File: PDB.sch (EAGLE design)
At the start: 66 parts

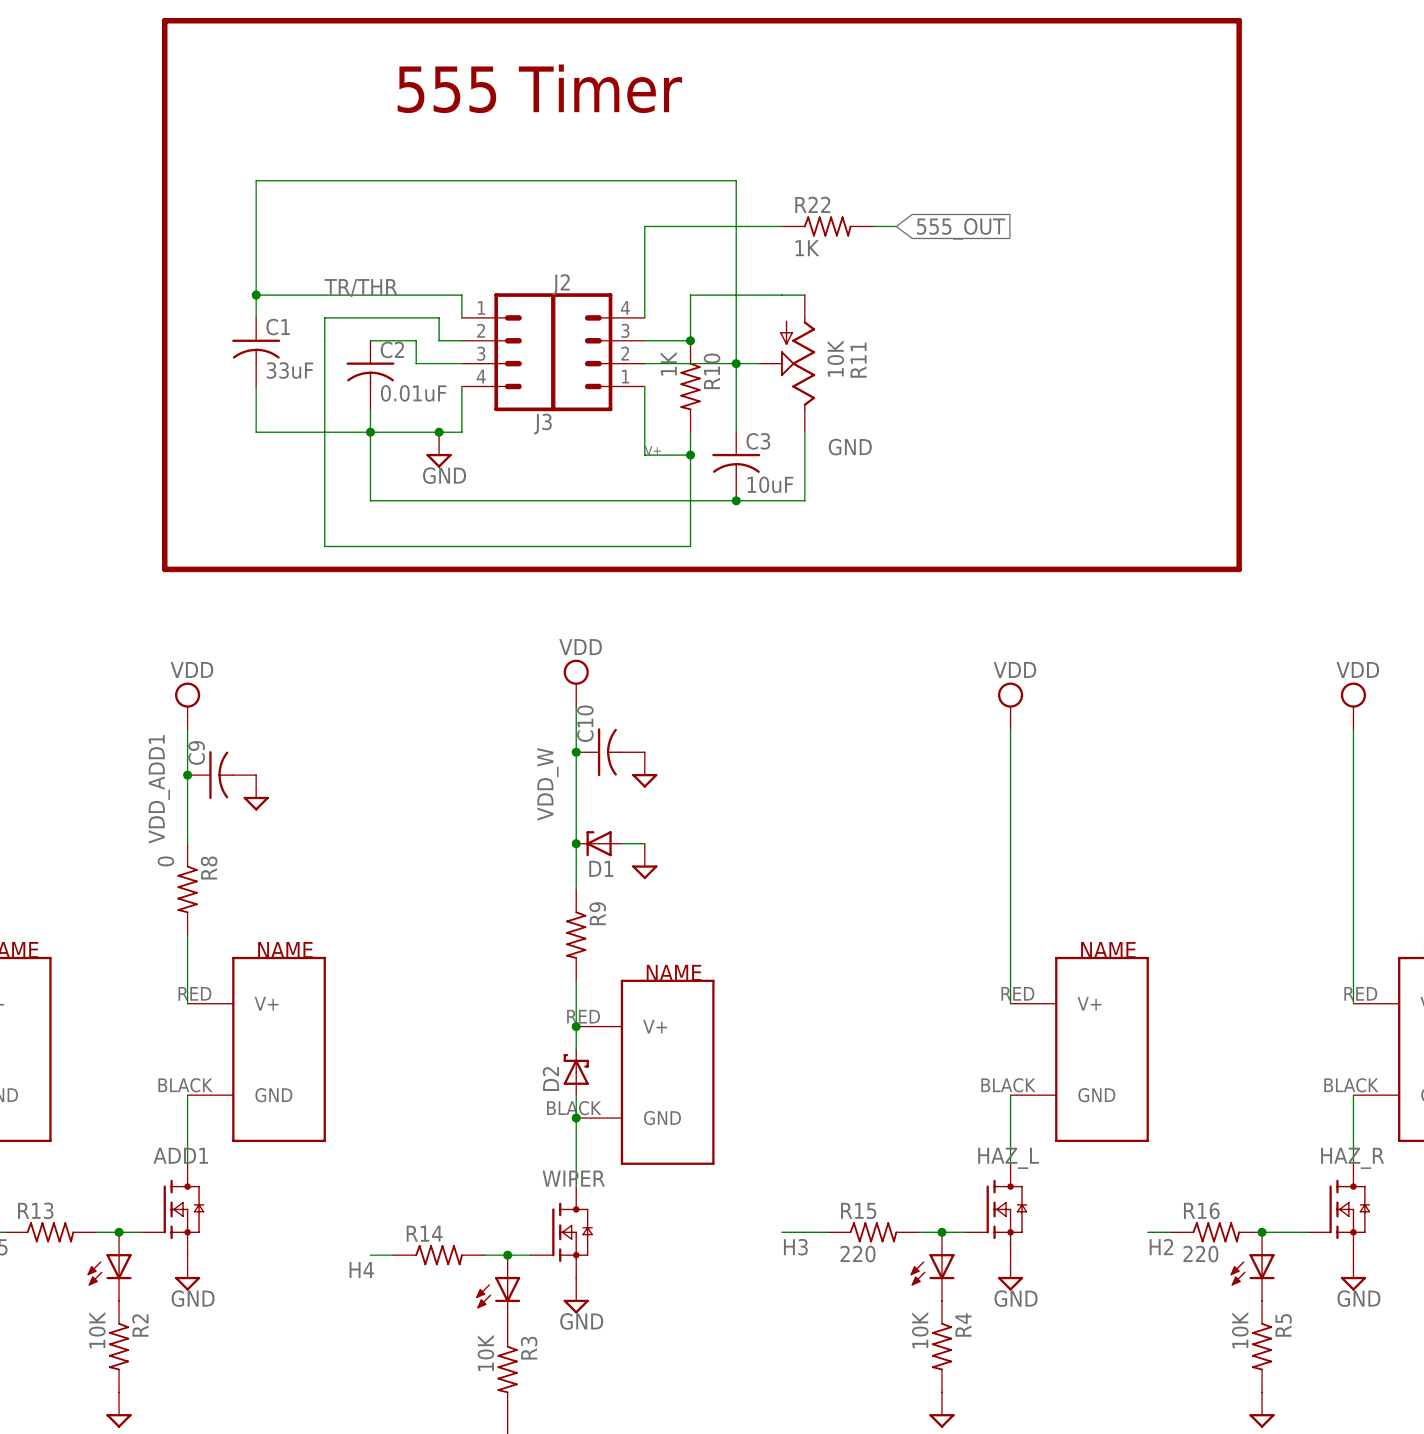
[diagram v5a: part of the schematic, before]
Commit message: modified ground plane in PDB
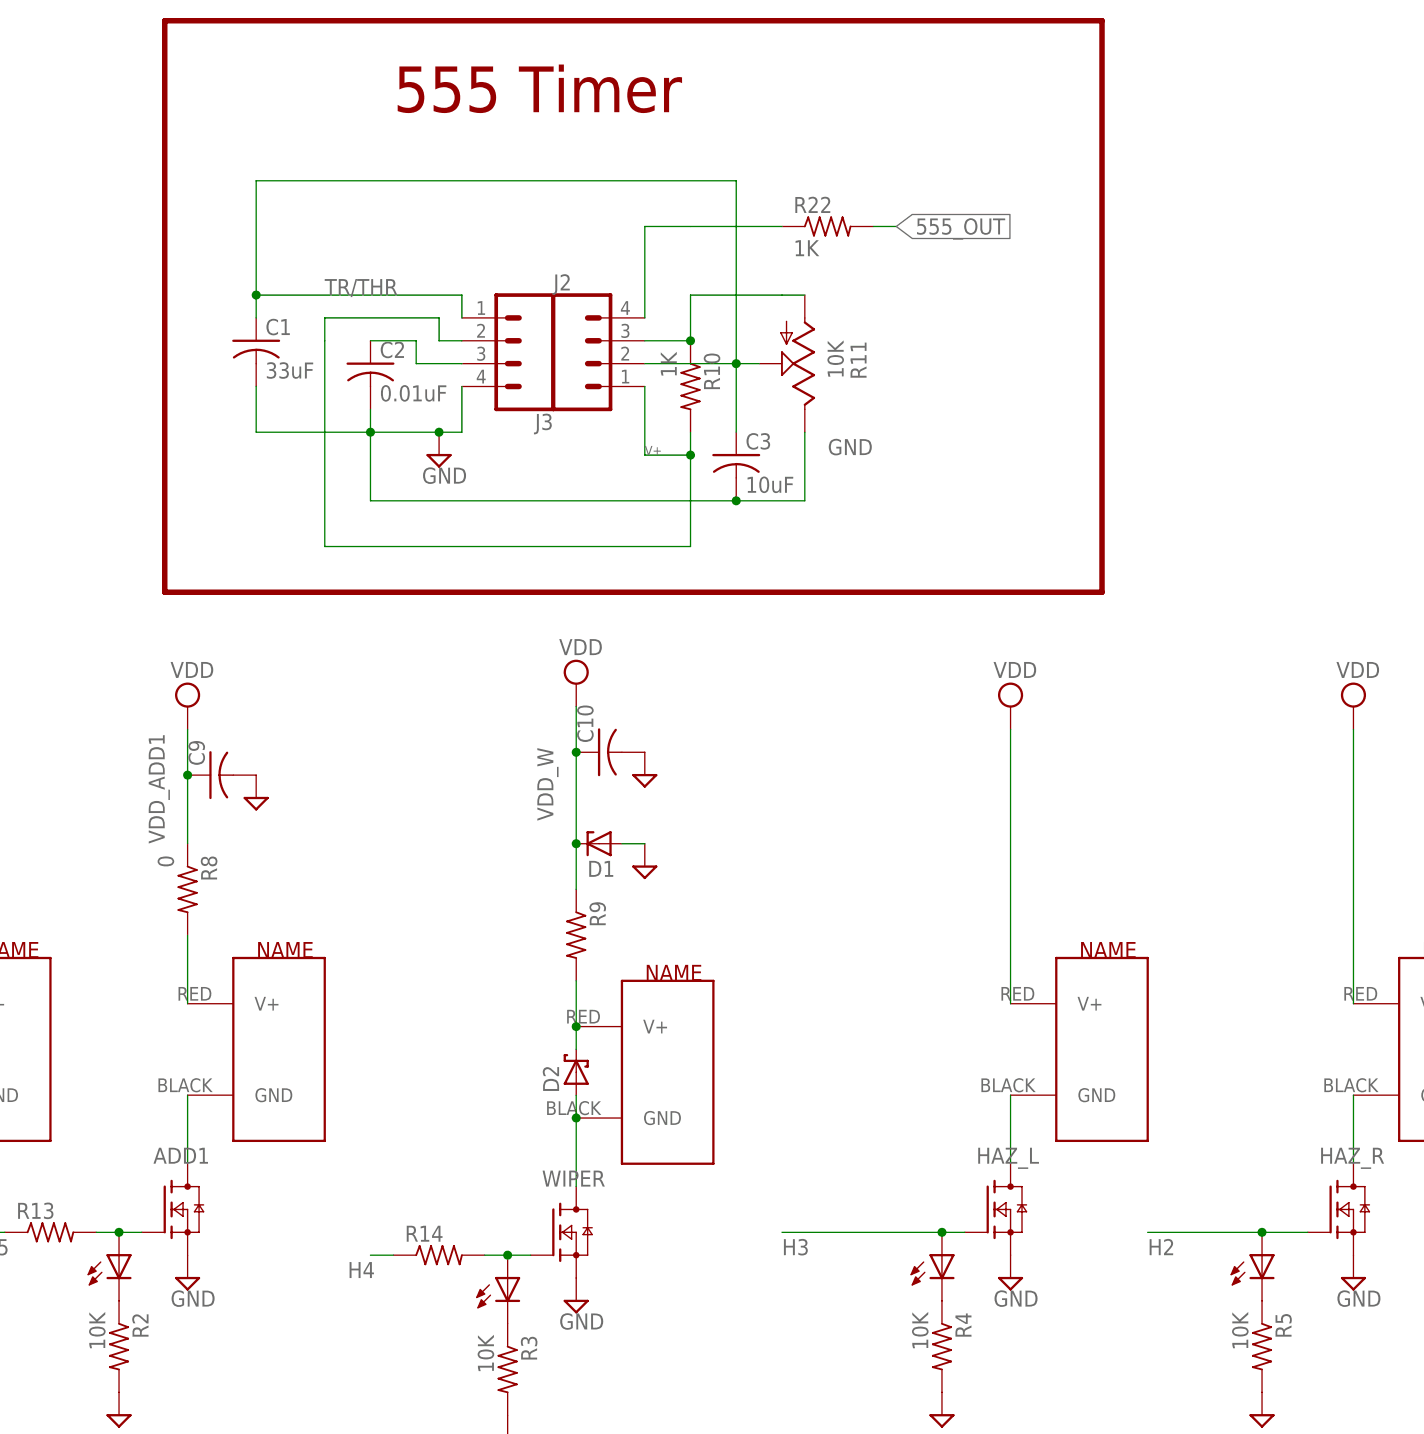
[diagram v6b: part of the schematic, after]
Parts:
- removed R15, R16: 220, rcl:R-US_R0805
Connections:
- removed net N$12: HAZ_R.G, LED5.A, R16.2
- removed net N$24: HAZ_L.G, LED4.A, R15.2
- net H2: now also HAZ_R.G, LED5.A; no longer R16.1
- net H3: now also HAZ_L.G, LED4.A; no longer R15.1
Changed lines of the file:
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@@
 <part name="R13" library="rcl" library_urn="urn:adsk.eagle:library:334" deviceset="R-US_" device="R0805" package3d_urn="urn:adsk.eagle:package:23553/2"/>
 <part name="R14" library="rcl" library_urn="urn:adsk.eagle:library:334" deviceset="R-US_" device="R0805" package3d_urn="urn:adsk.eagle:package:23553/2"/>
-<part name="R15" library="rcl" library_urn="urn:adsk.eagle:library:334" deviceset="R-US_" device="R0805" package3d_urn="urn:adsk.eagle:package:23553/2" value="220"/>
-<part name="R16" library="rcl" library_urn="urn:adsk.eagle:library:334" deviceset="R-US_" device="R0805" package3d_urn="urn:adsk.eagle:package:23553/2" value="220"/>
 <part name="R17" library="rcl" library_urn="urn:adsk.eagle:library:334" deviceset="R-US_" device="R0805" package3d_urn="urn:adsk.eagle:package:23553/2"/>
 <part name="R18" library="rcl" library_urn="urn:adsk.eagle:library:334" deviceset="R-US_" device="R0805" package3d_urn="urn:adsk.eagle:package:23553/2"/>
@@
 <description>Make a dock for the microcontroller</description>
 <plain>
-<wire x1="-30.48" y1="78.74" x2="-30.48" y2="139.7" width="0.6096" layer="94"/>
-<wire x1="-30.48" y1="139.7" x2="88.9" y2="139.7" width="0.6096" layer="94"/>
+<wire x1="-30.48" y1="76.2" x2="-30.48" y2="139.7" width="0.6096" layer="94"/>
+<wire x1="-30.48" y1="139.7" x2="73.66" y2="139.7" width="0.6096" layer="94"/>
 <text x="-5.08" y="129.54" size="5.08" layer="94">555 Timer</text>
 <text x="185.42" y="116.84" size="5.08" layer="94">12V IN</text>
@@
 <wire x1="-83.82" y1="-20.32" x2="-83.82" y2="-22.86" width="0.6096" layer="94"/>
 <text x="58.42" y="-48.26" size="5.08" layer="94">Switches</text>
-<wire x1="-30.48" y1="78.74" x2="88.9" y2="78.74" width="0.6096" layer="94"/>
-<wire x1="88.9" y1="78.74" x2="88.9" y2="139.7" width="0.6096" layer="94"/>
+<wire x1="-30.48" y1="76.2" x2="73.66" y2="76.2" width="0.6096" layer="94"/>
+<wire x1="73.66" y1="76.2" x2="73.66" y2="139.7" width="0.6096" layer="94"/>
 </plain>
 <instances>
@@
 <instance part="R13" gate="G$1" x="-43.18" y="5.08"/>
 <instance part="R14" gate="G$1" x="0" y="2.54"/>
-<instance part="R15" gate="G$1" x="48.26" y="5.08"/>
-<instance part="R16" gate="G$1" x="86.36" y="5.08"/>
 <instance part="R17" gate="G$1" x="121.92" y="5.08"/>
 <instance part="R18" gate="G$1" x="157.48" y="5.08"/>
@@
 </segment>
 <segment>
-<pinref part="R15" gate="G$1" pin="1"/>
-<wire x1="43.18" y1="5.08" x2="38.1" y2="5.08" width="0.1524" layer="91"/>
 <label x="38.1" y="2.54" size="1.778" layer="95"/>
+<pinref part="HAZ_L" gate="G$1" pin="G"/>
+<wire x1="58.42" y1="5.08" x2="55.88" y2="5.08" width="0.1524" layer="91"/>
+<pinref part="LED4" gate="G$1" pin="A"/>
+<junction x="55.88" y="5.08"/>
+<wire x1="38.1" y1="5.08" x2="55.88" y2="5.08" width="0.1524" layer="91"/>
 </segment>
 </net>
@@
 </segment>
 <segment>
-<pinref part="R16" gate="G$1" pin="1"/>
-<wire x1="81.28" y1="5.08" x2="78.74" y2="5.08" width="0.1524" layer="91"/>
 <label x="78.74" y="2.54" size="1.778" layer="95"/>
+<pinref part="HAZ_R" gate="G$1" pin="G"/>
+<pinref part="LED5" gate="G$1" pin="A"/>
+<wire x1="96.52" y1="5.08" x2="91.44" y2="5.08" width="0.1524" layer="91"/>
+<wire x1="78.74" y1="5.08" x2="91.44" y2="5.08" width="0.1524" layer="91"/>
+<junction x="91.44" y="5.08"/>
 </segment>
 </net>
@@
 </segment>
 </net>
-<net name="N$12" class="0">
-<segment>
-<pinref part="HAZ_R" gate="G$1" pin="G"/>
-<pinref part="R16" gate="G$1" pin="2"/>
-<pinref part="LED5" gate="G$1" pin="A"/>
-<wire x1="96.52" y1="5.08" x2="91.44" y2="5.08" width="0.1524" layer="91"/>
-<junction x="91.44" y="5.08"/>
-</segment>
-</net>
 <net name="N$13" class="0">
 <segment>
@@
 </segment>
 </net>
-<net name="N$24" class="0">
-<segment>
-<pinref part="HAZ_L" gate="G$1" pin="G"/>
-<pinref part="R15" gate="G$1" pin="2"/>
-<wire x1="58.42" y1="5.08" x2="55.88" y2="5.08" width="0.1524" layer="91"/>
-<pinref part="LED4" gate="G$1" pin="A"/>
-<junction x="55.88" y="5.08"/>
-<wire x1="55.88" y1="5.08" x2="53.34" y2="5.08" width="0.1524" layer="91"/>
-</segment>
-</net>

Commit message: cuck changes
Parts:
- removed J2, J3: (no value), SparkFun-Connectors:CONN_04LONGPADS
- added C4: 22uF, rcl:C-USC0805
- added IC1: LM555N, linear:LM555N
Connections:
- removed net V+: J2.1, J3.2, R10.2
- net CV: now also IC1.CV; no longer J3.3
- net DIS: now also IC1.DIS; no longer J2.3
- net GND: now also C4.2, IC1.GND; no longer J3.4
- net Q: now also IC1.Q; no longer J2.4
- net TR/THR: now also IC1.THR, IC1.TR; no longer J2.2, J3.1
- net VDD: now also C4.1, IC1.R, IC1.V+, R10.2
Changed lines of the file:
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@@
 <part name="C3" library="rcl" library_urn="urn:adsk.eagle:library:334" deviceset="C-US" device="C0805K" package3d_urn="urn:adsk.eagle:package:23681/2" value="10uF"/>
 <part name="R11" library="pot" library_urn="urn:adsk.eagle:library:331" deviceset="TRIM_US-" device="B25U" package3d_urn="urn:adsk.eagle:package:22685/1" value="10K"/>
-<part name="J2" library="SparkFun-Connectors" library_urn="urn:adsk.eagle:library:513" deviceset="CONN_04" device="LONGPADS" package3d_urn="urn:adsk.eagle:package:38098/1"/>
-<part name="J3" library="SparkFun-Connectors" library_urn="urn:adsk.eagle:library:513" deviceset="CONN_04" device="LONGPADS" package3d_urn="urn:adsk.eagle:package:38098/1"/>
+<part name="IC1" library="linear" library_urn="urn:adsk.eagle:library:262" deviceset="*555" device="N" package3d_urn="urn:adsk.eagle:package:16409/2" technology="LM"/>
+<part name="C4" library="rcl" library_urn="urn:adsk.eagle:library:334" deviceset="C-US" device="C0805" package3d_urn="urn:adsk.eagle:package:23617/2" value="22uF"/>
 </parts>
 <sheets>
@@
 <instance part="C3" gate="G$1" x="33.02" y="91.44"/>
 <instance part="R11" gate="G$1" x="40.64" y="101.6" rot="R180"/>
-<instance part="J2" gate="G$1" x="17.78" y="101.6"/>
-<instance part="J3" gate="G$1" x="7.62" y="104.14" rot="R180"/>
+<instance part="IC1" gate="A" x="12.7" y="101.6"/>
+<instance part="C4" gate="G$1" x="-17.78" y="88.9" rot="R180"/>
 </instances>
 <busses>
@@
 </segment>
 <segment>
-<pinref part="J3" gate="G$1" pin="4"/>
-<wire x1="2.54" y1="93.98" x2="2.54" y2="99.06" width="0.1524" layer="91"/>
 <wire x1="2.54" y1="93.98" x2="0" y2="93.98" width="0.1524" layer="91"/>
 <pinref part="GND6" gate="GND" pin="GND"/>
@@
 <wire x1="-20.32" y1="99.06" x2="-20.32" y2="93.98" width="0.1524" layer="91"/>
 <junction x="-7.62" y="93.98"/>
-<wire x1="-20.32" y1="93.98" x2="-7.62" y2="93.98" width="0.1524" layer="91"/>
+<wire x1="-20.32" y1="93.98" x2="-17.78" y2="93.98" width="0.1524" layer="91"/>
+<wire x1="-17.78" y1="93.98" x2="-7.62" y2="93.98" width="0.1524" layer="91"/>
 <wire x1="-7.62" y1="93.98" x2="0" y2="93.98" width="0.1524" layer="91"/>
 <junction x="0" y="93.98"/>
+<pinref part="IC1" gate="A" pin="GND"/>
+<pinref part="C4" gate="G$1" pin="2"/>
+<junction x="-17.78" y="93.98"/>
 </segment>
 <segment>
@@
 <pinref part="SUPPLY16" gate="G$1" pin="VDD"/>
 </segment>
+<segment>
+<pinref part="R10" gate="G$1" pin="2"/>
+<wire x1="-12.7" y1="106.68" x2="-12.7" y2="86.36" width="0.1524" layer="91"/>
+<wire x1="-12.7" y1="86.36" x2="-12.7" y2="81.28" width="0.1524" layer="91"/>
+<wire x1="-12.7" y1="81.28" x2="27.94" y2="81.28" width="0.1524" layer="91"/>
+<wire x1="27.94" y1="81.28" x2="27.94" y2="93.98" width="0.1524" layer="91"/>
+<wire x1="-12.7" y1="106.68" x2="0" y2="106.68" width="0.1524" layer="91"/>
+<wire x1="0" y1="106.68" x2="0" y2="104.14" width="0.1524" layer="91"/>
+<wire x1="0" y1="104.14" x2="2.54" y2="104.14" width="0.1524" layer="91"/>
+<label x="22.86" y="91.44" size="1.016" layer="95"/>
+<wire x1="22.86" y1="93.98" x2="27.94" y2="93.98" width="0.1524" layer="91"/>
+<junction x="27.94" y="93.98"/>
+<pinref part="IC1" gate="A" pin="R"/>
+<pinref part="IC1" gate="A" pin="V+"/>
+<pinref part="C4" gate="G$1" pin="1"/>
+<wire x1="-17.78" y1="86.36" x2="-12.7" y2="86.36" width="0.1524" layer="91"/>
+<junction x="-12.7" y="86.36"/>
+</segment>
 </net>
 <net name="N$8" class="0">
@@
 </segment>
 </net>
-<net name="V+" class="0">
-<segment>
-<pinref part="R10" gate="G$1" pin="2"/>
-<wire x1="-12.7" y1="104.14" x2="-12.7" y2="81.28" width="0.1524" layer="91"/>
-<wire x1="-12.7" y1="81.28" x2="27.94" y2="81.28" width="0.1524" layer="91"/>
-<wire x1="27.94" y1="81.28" x2="27.94" y2="91.44" width="0.1524" layer="91"/>
-<pinref part="J3" gate="G$1" pin="2"/>
-<wire x1="27.94" y1="91.44" x2="27.94" y2="93.98" width="0.1524" layer="91"/>
-<wire x1="-12.7" y1="104.14" x2="-12.7" y2="106.68" width="0.1524" layer="91"/>
-<wire x1="-12.7" y1="106.68" x2="0" y2="106.68" width="0.1524" layer="91"/>
-<wire x1="0" y1="106.68" x2="0" y2="104.14" width="0.1524" layer="91"/>
-<wire x1="0" y1="104.14" x2="2.54" y2="104.14" width="0.1524" layer="91"/>
-<pinref part="J2" gate="G$1" pin="1"/>
-<wire x1="22.86" y1="91.44" x2="22.86" y2="99.06" width="0.1524" layer="91"/>
-<label x="22.86" y="91.44" size="1.016" layer="95"/>
-<wire x1="22.86" y1="91.44" x2="27.94" y2="91.44" width="0.1524" layer="91"/>
-<junction x="27.94" y="91.44"/>
-</segment>
-</net>
 <net name="DIS" class="0">
 <segment>
 <pinref part="R10" gate="G$1" pin="1"/>
 <wire x1="27.94" y1="104.14" x2="27.94" y2="109.22" width="0.1524" layer="91"/>
-<wire x1="27.94" y1="109.22" x2="38.1" y2="109.22" width="0.1524" layer="91"/>
+<wire x1="27.94" y1="109.22" x2="40.64" y2="109.22" width="0.1524" layer="91"/>
 <pinref part="R11" gate="G$1" pin="A"/>
-<wire x1="38.1" y1="109.22" x2="40.64" y2="109.22" width="0.1524" layer="91"/>
-<pinref part="J2" gate="G$1" pin="3"/>
 <wire x1="22.86" y1="104.14" x2="27.94" y2="104.14" width="0.1524" layer="91"/>
 <junction x="27.94" y="104.14"/>
+<pinref part="IC1" gate="A" pin="DIS"/>
 </segment>
 </net>
@@
 <segment>
 <pinref part="C2" gate="G$1" pin="1"/>
-<wire x1="-2.54" y1="101.6" x2="-2.54" y2="104.14" width="0.1524" layer="91"/>
+<wire x1="-2.54" y1="99.06" x2="-2.54" y2="104.14" width="0.1524" layer="91"/>
 <wire x1="-2.54" y1="104.14" x2="-7.62" y2="104.14" width="0.1524" layer="91"/>
-<pinref part="J3" gate="G$1" pin="3"/>
-<wire x1="-2.54" y1="101.6" x2="2.54" y2="101.6" width="0.1524" layer="91"/>
+<wire x1="-2.54" y1="99.06" x2="2.54" y2="99.06" width="0.1524" layer="91"/>
+<pinref part="IC1" gate="A" pin="CV"/>
 </segment>
 </net>
 <net name="Q" class="0">
 <segment>
-<wire x1="22.86" y1="106.68" x2="22.86" y2="116.84" width="0.1524" layer="91"/>
+<wire x1="22.86" y1="109.22" x2="22.86" y2="116.84" width="0.1524" layer="91"/>
 <pinref part="R22" gate="G$1" pin="1"/>
-<wire x1="22.86" y1="116.84" x2="27.94" y2="116.84" width="0.1524" layer="91"/>
-<wire x1="27.94" y1="116.84" x2="38.1" y2="116.84" width="0.1524" layer="91"/>
-<pinref part="J2" gate="G$1" pin="4"/>
+<wire x1="22.86" y1="116.84" x2="38.1" y2="116.84" width="0.1524" layer="91"/>
+<pinref part="IC1" gate="A" pin="Q"/>
 </segment>
 </net>
@@
 <junction x="-20.32" y="109.22"/>
 <wire x1="-20.32" y1="121.92" x2="33.02" y2="121.92" width="0.1524" layer="91"/>
-<wire x1="33.02" y1="121.92" x2="33.02" y2="101.6" width="0.1524" layer="91"/>
-<wire x1="33.02" y1="101.6" x2="27.94" y2="101.6" width="0.1524" layer="91"/>
-<wire x1="27.94" y1="101.6" x2="22.86" y2="101.6" width="0.1524" layer="91"/>
+<wire x1="33.02" y1="121.92" x2="33.02" y2="99.06" width="0.1524" layer="91"/>
+<wire x1="33.02" y1="99.06" x2="22.86" y2="99.06" width="0.1524" layer="91"/>
 <pinref part="C3" gate="G$1" pin="1"/>
-<wire x1="33.02" y1="101.6" x2="33.02" y2="93.98" width="0.1524" layer="91"/>
-<junction x="33.02" y="101.6"/>
+<wire x1="33.02" y1="99.06" x2="33.02" y2="93.98" width="0.1524" layer="91"/>
+<junction x="33.02" y="99.06"/>
 <label x="-12.7" y="109.22" size="1.778" layer="95"/>
 <pinref part="R11" gate="G$1" pin="S"/>
-<wire x1="35.56" y1="101.6" x2="33.02" y2="101.6" width="0.1524" layer="91"/>
-<pinref part="J2" gate="G$1" pin="2"/>
-<pinref part="J3" gate="G$1" pin="1"/>
-<wire x1="2.54" y1="109.22" x2="2.54" y2="106.68" width="0.1524" layer="91"/>
-</segment>
-</net>
+<wire x1="35.56" y1="101.6" x2="33.02" y2="99.06" width="0.1524" layer="91"/>
+<pinref part="IC1" gate="A" pin="TR"/>
+<pinref part="IC1" gate="A" pin="THR"/>
+</segment>
+</net>
